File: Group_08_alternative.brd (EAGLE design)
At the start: 62.2 x 82.5 mm, 29 parts, among them J1 POWER_JACKPTH_LOCK, U1 +12v, U3 TCA9546ATSSOP, U4 TMUX1208

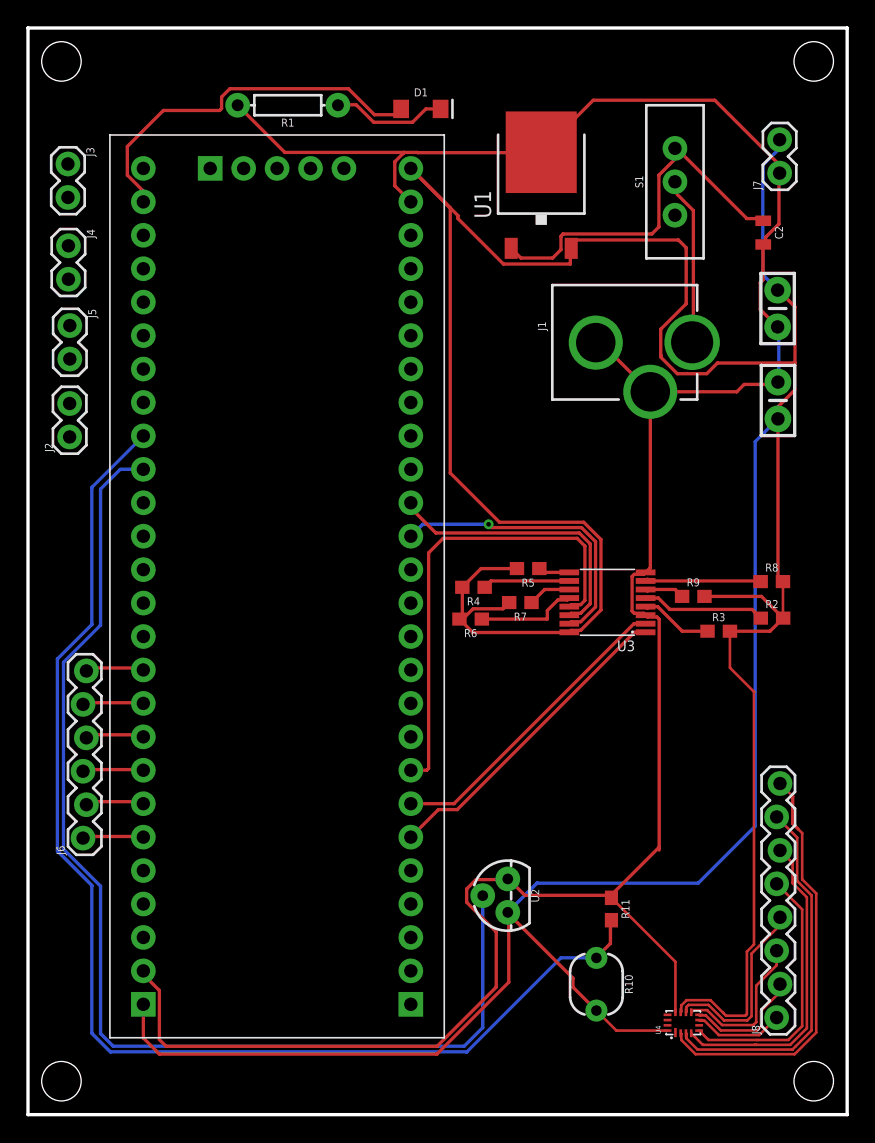
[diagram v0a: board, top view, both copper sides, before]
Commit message: Optimized board, added silkscreen. 0 errors after performing DCR.
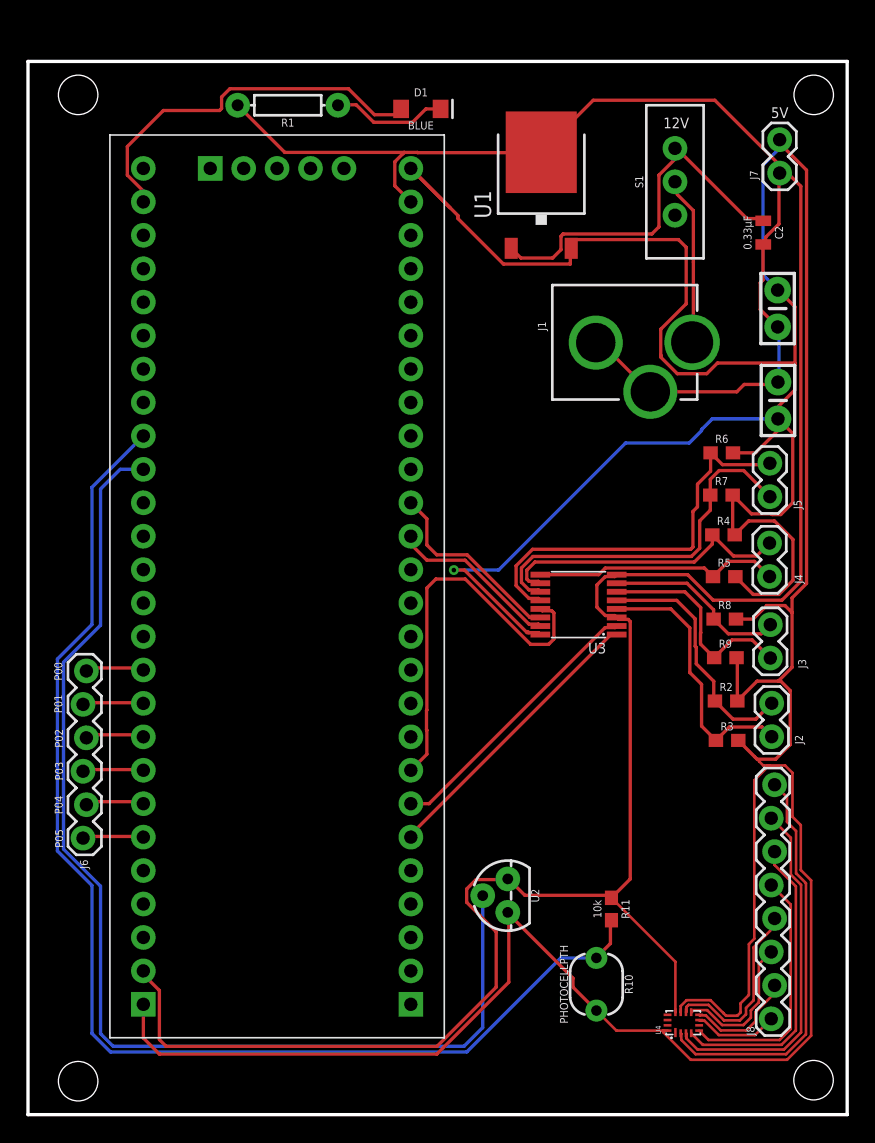
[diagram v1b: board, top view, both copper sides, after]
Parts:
- moved J3 65.2 mm to (56.4, 34.7), turned to 90 degrees
- moved J4 58.9 mm to (56.3, 40.9), turned to 90 degrees
- moved J2 58.0 mm to (56.5, 28.7)
- moved J5 54.7 mm to (56.4, 46.9), turned to 90 degrees
- moved R6 22.9 mm to (52.7, 50.3), turned to 0 degrees
- moved R4 19.4 mm to (52.8, 44.0), turned to 0 degrees
- moved R7 17.3 mm to (52.7, 47.1), turned to 0 degrees
- moved R5 14.9 mm to (52.9, 40.9), turned to 0 degrees
- moved R3 8.32 mm to (53.1, 28.4)
- moved R2 7.20 mm to (53.0, 31.4)
- moved R9 5.26 mm to (53.0, 34.7)
- moved R8 4.57 mm to (52.9, 37.6)
- moved U3 2.21 mm to (41.8, 38.7)
- moved J8 0.42 mm to (56.6, 7.28)
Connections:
- removed net N$1: R2.1, U3.5
- removed net N$3: R3.1, U3.4
- removed net N$4: R8.1, U3.7
- removed net N$5: R9.1, U3.6
- removed net N$6: R4.1, U3.10
- removed net N$7: R5.1, U3.9
- removed net N$8: R6.1, U3.12
- removed net N$9: R7.1, U3.11
- net I2C_SCL_0: now also R2.1, U3.5
- net I2C_SCL_1: now also R8.1, U3.7
- net I2C_SCL_2: now also R4.1, U3.10
- net I2C_SCL_3: now also R6.1, U3.12
- net I2C_SDA_0: now also R3.1, U3.4
- net I2C_SDA_1: now also R9.1, U3.6
- net I2C_SDA_2: now also R5.1, U3.9
- net I2C_SDA_3: now also R7.1, U3.11
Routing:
- net GND: track 192.8 -> 226.0 mm
- net I2C_SCL_3: track 0.00 -> 30.5 mm
- net I2C_SDA_3: track 0.00 -> 28.2 mm
- net 5V: track 306.9 -> 330.9 mm, vias 0 -> 1
- net I2C_SCL_2: track 0.00 -> 22.9 mm
- net I2C_SDA_0: track 0.00 -> 20.5 mm
- net I2C_SDA_2: track 0.00 -> 18.9 mm
- net I2C_SCL_0: track 0.00 -> 18.8 mm
- net I2C_SDA_1: track 0.00 -> 16.5 mm
- net I2C_SCL_1: track 0.00 -> 14.0 mm
- net I2C_SDA: track 22.4 -> 13.0 mm, vias 1 -> 0
- net N$1: track 9.38 -> 0.00 mm
- net N$4: track 9.24 -> 0.00 mm
- net N$8: track 7.69 -> 0.00 mm
- net I2C_SCL: track 21.6 -> 14.6 mm
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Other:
- board size 62.2 x 82.5 mm -> 62.2 x 80 mm
- board text added: "12V"
- board text added: "5V"
- board text added: "P00"
- board text added: "P01"
- board text added: "P02"
- board text added: "P03"
- board text added: "P04"
- board text added: "P05"
